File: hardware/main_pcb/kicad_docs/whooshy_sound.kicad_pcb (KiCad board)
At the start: 4 copper layers, 83.8 x 80 mm, 122 parts, among them J1 audio_in, J10 SWD_header, J11 LED_switch, J2 audio_out, J3 extern_cutoff_CV_TRS, J4 extern_rez_CV_TRS, J5 9VDC_in, J6 signal_in, J7 signal_out, J8 cutoff_CV_in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

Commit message: tidy up main board
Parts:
- moved R10 1.12 mm to (149.2, 83.9)
- moved R16 1.10 mm to (159.4, 83.9)
- moved C24 0.63 mm to (144.8, 130.2)
- moved U5 0.20 mm to (169.1, 113.2)
- moved U6 0.13 mm to (169.0, 92.1)
- moved U7 0.06 mm to (193.1, 104.1)
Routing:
- net /cutoff_CV_generator/LFO/shape_CV: track 72.7 -> 69.5 mm
- net -12V: track 197.0 -> 199.2 mm
- net /input_buffer/raw_dry_signal_in: track 12.8 -> 14.4 mm
- net +12V: track 136.1 -> 137.3 mm
- net Net-(R10-Pad1): track 72.2 -> 71.1 mm
- net /resonance_CV_generator/expression_pedal_ring_current: track 7.62 -> 8.74 mm
- net Net-(R16-Pad1): track 66.2 -> 65.1 mm
- net /cutoff_CV_generator/expression_pedal_ring_current: track 7.62 -> 8.72 mm
- net Net-(R33-Pad1): track 72.6 -> 73.3 mm
- net Net-(C32-Pad1): track 76.2 -> 76.8 mm
- net Net-(C28-Pad1): track 55.7 -> 56.2 mm

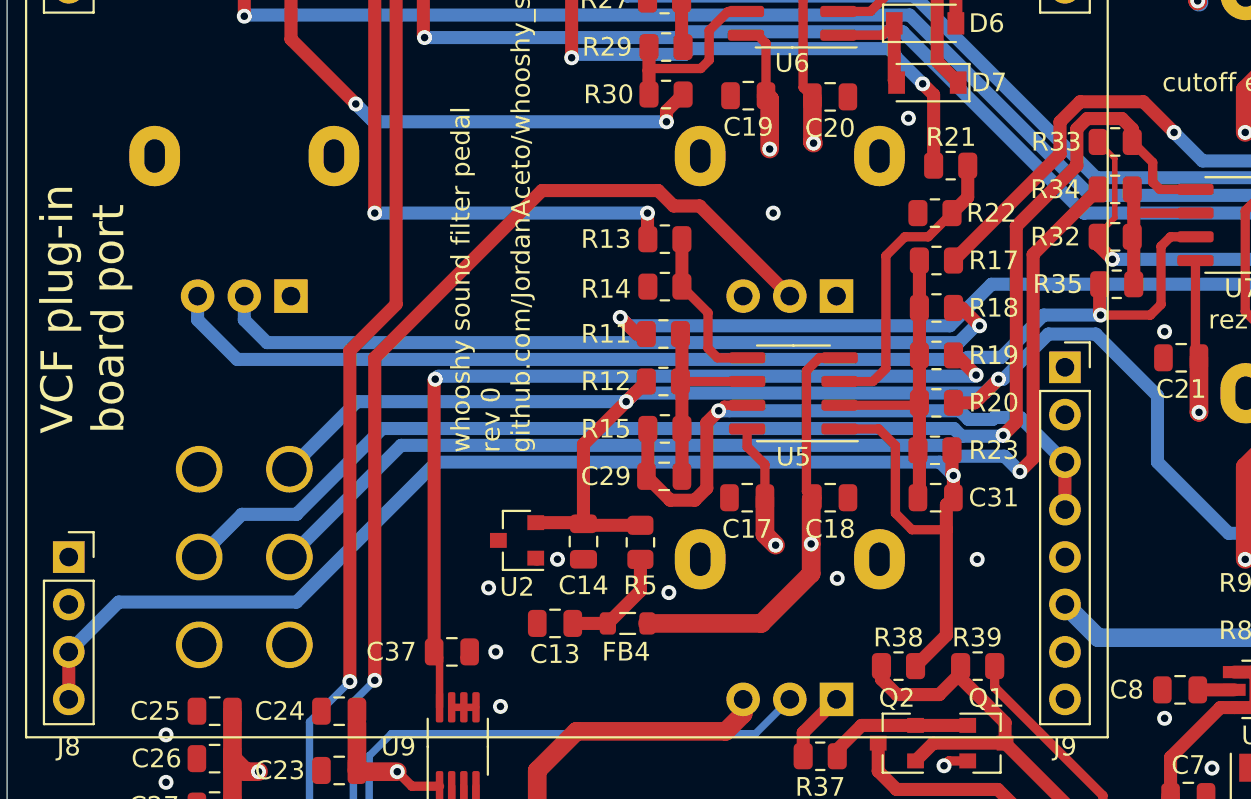
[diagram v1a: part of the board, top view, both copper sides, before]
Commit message: flip env invert switch, condense cap types
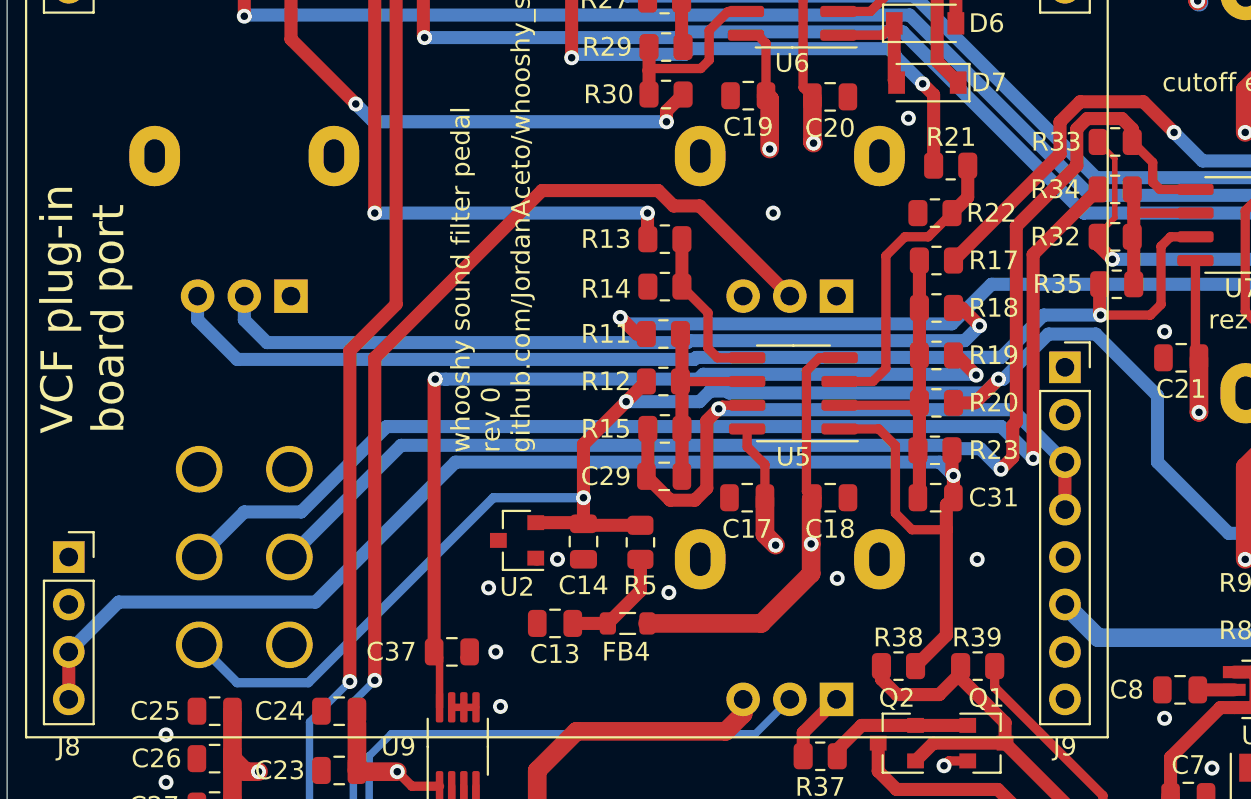
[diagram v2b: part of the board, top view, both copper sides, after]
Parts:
- C25: value 2u2 -> 10u
- C6: value 10n -> 100n
- C8: value 47n -> 100n
- R3: value 560 -> 1k
- turned SW1 to 0 degrees
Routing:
- net -5V: track 103.3 -> 109.4 mm, vias 2 -> 3
- net Net-(R34-Pad2): track 59.0 -> 64.1 mm
- net Net-(R33-Pad1): track 73.3 -> 70.2 mm

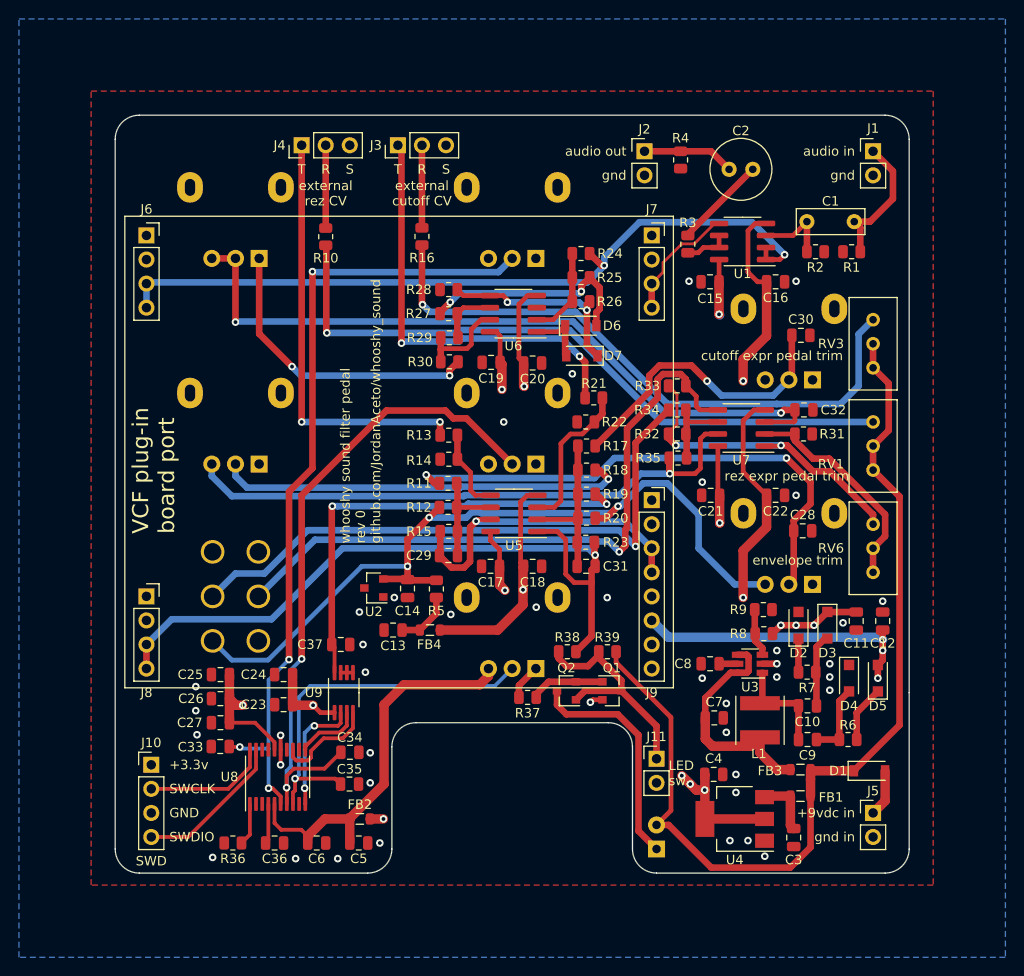
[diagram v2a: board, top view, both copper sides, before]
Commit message: center envelope follower around +1v, tidy up
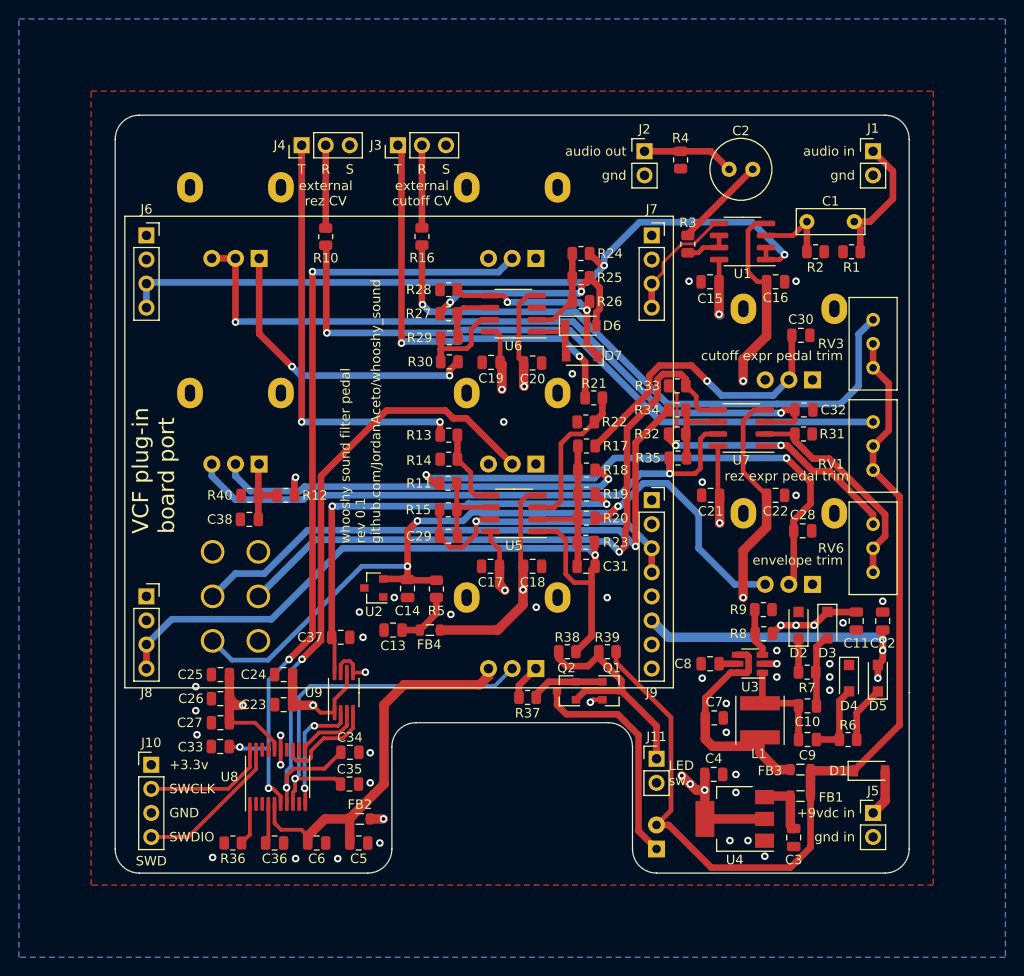
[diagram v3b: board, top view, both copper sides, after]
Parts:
- added C38: 10u, Capacitor_SMD:C_0805_2012Metric, F.Cu at (141.2, 113.8)
- added R40: 1k2, Resistor_SMD:R_0805_2012Metric, F.Cu at (141.2, 111.3)
- C2: value 10u -> 10u np
- R12: value 560k -> 2k7
- R13: value 82k -> 68k
- R14: value 18k -> 27k
- R20: value 560k -> 270k
- R21: value 82k -> 120k
- R22: value 18k -> 15k
- R3, R30: value 1k -> 1k2
- RV7: value 10k -> 100k
- moved R12 17.2 mm to (145.0, 111.3), turned to 0 degrees
- moved R15 2.29 mm to (162.2, 112.8)
- moved C29 2.03 mm to (162.2, 115.6)
- moved C37 0.76 mm to (150.8, 126.2)
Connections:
- R12 pad 1: Net-(C29-Pad2) -> Net-(C38-Pad1)
- R12 pad 2: -5V -> +3.3VA
- RV7 pad 1: GND -> Net-(C38-Pad1)
- U9 pad 6: GND -> +3V3
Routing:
- net +3.3VA: track 84.5 -> 107.4 mm, vias 0 -> 1
- net Net-(C38-Pad1): track 0.00 -> 7.86 mm
- net +3V3: track 117.4 -> 122.2 mm
- net GND: track 11.9 -> 14.8 mm
- net /resonance_CV_generator/summed_resonance_CV_out: track 35.0 -> 32.9 mm
- net Net-(C29-Pad2): track 11.2 -> 9.40 mm
- net -5V: track 109.4 -> 108.4 mm
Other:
- board text added: "whooshy sound filter pedal rev 0.1 github.com/JordanAceto/whooshy_sound"
- board text removed: "whooshy sound filter pedal rev 0 github.com/JordanAceto/whooshy_sound"
